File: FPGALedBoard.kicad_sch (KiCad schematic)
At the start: 5 parts, among them J1 Conn_02x20_Odd_Even

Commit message: Placa roeada automaticamente.
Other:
- company: (none) -> IFTM - Campus Ituiutaba
- title: (none) -> FPGA LED Output Board - Main
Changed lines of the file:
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@@
 (kicad_sch (version 20211123) (generator eeschema)
   (paper "A4")
+  (title_block
+    (title "FPGA LED Output Board - Main")
+    (date "2022-01-26")
+    (rev "1")
+    (company "IFTM - Campus Ituiutaba")
+  )
   (junction (at 176.53 71.12) (diameter 0) (color 0 0 0 0)
   )
@@
       (reference "#PWR0105") (unit 1) (value "+5V") (footprint "")
     )
+    (path "/ebb9e051-9d57-48fe-a44a-4edf58ab7acf/20d3631c-a610-485d-a77f-480404a55a4f"
+      (reference "#PWR0106") (unit 1) (value "GND") (footprint "")
+    )
+    (path "/ebb9e051-9d57-48fe-a44a-4edf58ab7acf/147d8636-f8cb-4d9a-9fe2-4658fd953f44"
+      (reference "#PWR0107") (unit 1) (value "+5V") (footprint "")
+    )
+    (path "/ebb9e051-9d57-48fe-a44a-4edf58ab7acf/99e75819-1ee6-4118-be75-84e1bafd18ae"
+      (reference "#PWR0108") (unit 1) (value "GND") (footprint "")
+    )
+    (path "/ebb9e051-9d57-48fe-a44a-4edf58ab7acf/51f6e505-70fe-4cfa-8e51-aa721df03c0b"
+      (reference "#PWR0109") (unit 1) (value "+5V") (footprint "")
+    )
+    (path "/b1f06ebd-9631-4b3b-9237-63ceeafca95e/b8bb4a94-4aef-4d3f-bdd0-866eb8c04d91"
+      (reference "C1") (unit 1) (value "10uF") (footprint "Capacitor_THT:CP_Radial_D5.0mm_P2.50mm")
+    )
+    (path "/b1f06ebd-9631-4b3b-9237-63ceeafca95e/dadc5b33-c8b6-468e-bb36-9ffa3f059f37"
+      (reference "C2") (unit 1) (value "10uF") (footprint "Capacitor_THT:CP_Radial_D5.0mm_P2.50mm")
+    )
+    (path "/b1f06ebd-9631-4b3b-9237-63ceeafca95e/4dff0a8e-15b6-4ad4-9af2-e1592dfea4bc"
+      (reference "C3") (unit 1) (value "10uF") (footprint "Capacitor_THT:CP_Radial_D5.0mm_P2.50mm")
+    )
+    (path "/ebb9e051-9d57-48fe-a44a-4edf58ab7acf/ada4f1f9-a877-4a31-ac0e-674903a1c441"
+      (reference "C4") (unit 1) (value "10uF") (footprint "Capacitor_THT:CP_Radial_D5.0mm_P2.50mm")
+    )
+    (path "/ebb9e051-9d57-48fe-a44a-4edf58ab7acf/fee69415-3b1b-467a-9596-a7af933deba2"
+      (reference "C5") (unit 1) (value "10uF") (footprint "Capacitor_THT:CP_Radial_D5.0mm_P2.50mm")
+    )
     (path "/b1f06ebd-9631-4b3b-9237-63ceeafca95e/bafb552e-736d-4d46-943b-7a792067c0dd"
       (reference "D1") (unit 1) (value "LED") (footprint "LED_THT:LED_D3.0mm")
@@
       (reference "U3") (unit 4) (value "74AHC04") (footprint "Package_DIP:DIP-14_W7.62mm")
     )
+    (path "/ebb9e051-9d57-48fe-a44a-4edf58ab7acf/8f177dae-7048-44cb-aed5-9ee2ed31b985"
+      (reference "U3") (unit 5) (value "74AHC04") (footprint "Package_DIP:DIP-14_W7.62mm")
+    )
+    (path "/ebb9e051-9d57-48fe-a44a-4edf58ab7acf/e32c4ea7-4f7f-485c-bc9d-52c3c4186a99"
+      (reference "U3") (unit 6) (value "74AHC04") (footprint "Package_DIP:DIP-14_W7.62mm")
+    )
     (path "/b1f06ebd-9631-4b3b-9237-63ceeafca95e/94419dcd-8a47-4346-bad9-959b3a1cf43c"
       (reference "U3") (unit 7) (value "74AHC04") (footprint "Package_DIP:DIP-14_W7.62mm")
@@
       (reference "U4") (unit 4) (value "74AHC04") (footprint "Package_DIP:DIP-14_W7.62mm")
     )
-    (path "/ebb9e051-9d57-48fe-a44a-4edf58ab7acf/8f177dae-7048-44cb-aed5-9ee2ed31b985"
+    (path "/ebb9e051-9d57-48fe-a44a-4edf58ab7acf/9775dbd4-51ad-4918-bcc6-fc67cc365ee7"
       (reference "U4") (unit 5) (value "74AHC04") (footprint "Package_DIP:DIP-14_W7.62mm")
     )
-    (path "/ebb9e051-9d57-48fe-a44a-4edf58ab7acf/e32c4ea7-4f7f-485c-bc9d-52c3c4186a99"
+    (path "/ebb9e051-9d57-48fe-a44a-4edf58ab7acf/d05b7b76-e8d1-4210-8cd0-720f16e13d24"
       (reference "U4") (unit 6) (value "74AHC04") (footprint "Package_DIP:DIP-14_W7.62mm")
+    )
+    (path "/ebb9e051-9d57-48fe-a44a-4edf58ab7acf/f01717ce-5ea2-40bb-b345-2f1eb154ce2d"
+      (reference "U4") (unit 7) (value "74AHC04") (footprint "Package_DIP:DIP-14_W7.62mm")
     )
     (path "/ebb9e051-9d57-48fe-a44a-4edf58ab7acf/cfc3b2b4-1d97-4f46-b5dc-f14c71e1a6a2"
@@
       (reference "U5") (unit 4) (value "74AHC04") (footprint "Package_DIP:DIP-14_W7.62mm")
     )
-    (path "/ebb9e051-9d57-48fe-a44a-4edf58ab7acf/9775dbd4-51ad-4918-bcc6-fc67cc365ee7"
+    (path "/ebb9e051-9d57-48fe-a44a-4edf58ab7acf/f1165d29-5632-40a1-b10d-a3067f0b2b0a"
       (reference "U5") (unit 5) (value "74AHC04") (footprint "Package_DIP:DIP-14_W7.62mm")
     )
-    (path "/ebb9e051-9d57-48fe-a44a-4edf58ab7acf/d05b7b76-e8d1-4210-8cd0-720f16e13d24"
+    (path "/ebb9e051-9d57-48fe-a44a-4edf58ab7acf/c888f29d-e025-449f-a4a4-edeed2746fde"
       (reference "U5") (unit 6) (value "74AHC04") (footprint "Package_DIP:DIP-14_W7.62mm")
+    )
+    (path "/ebb9e051-9d57-48fe-a44a-4edf58ab7acf/aebbe4a9-8276-47f3-ab49-db454bafd386"
+      (reference "U5") (unit 7) (value "74AHC04") (footprint "Package_DIP:DIP-14_W7.62mm")
     )
     (path "/ebb9e051-9d57-48fe-a44a-4edf58ab7acf/0256fd15-c8e3-42ff-8a02-4ab7ec7ac551"
       (reference "U6") (unit 1) (value "D148K") (footprint "Display_7Segment:D1X8K")
     )
-    (path "/ebb9e051-9d57-48fe-a44a-4edf58ab7acf/f1165d29-5632-40a1-b10d-a3067f0b2b0a"
-      (reference "U7") (unit 5) (value "74AHC04") (footprint "Package_DIP:DIP-14_W7.62mm")
-    )
-    (path "/ebb9e051-9d57-48fe-a44a-4edf58ab7acf/c888f29d-e025-449f-a4a4-edeed2746fde"
-      (reference "U7") (unit 6) (value "74AHC04") (footprint "Package_DIP:DIP-14_W7.62mm")
-    )
     (path "/ebb9e051-9d57-48fe-a44a-4edf58ab7acf/cc5a93cc-9281-4348-a8ca-ccf4c4a00ed9"

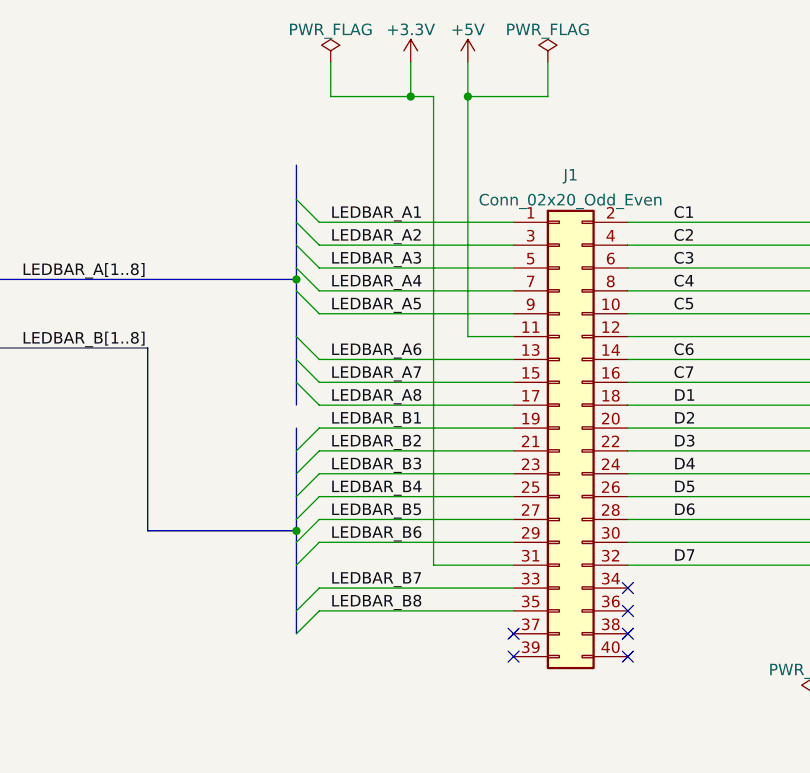
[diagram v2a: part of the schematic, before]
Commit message: Corrigido um erro na linha de 3.3V. Adicionado o Ground Plane.
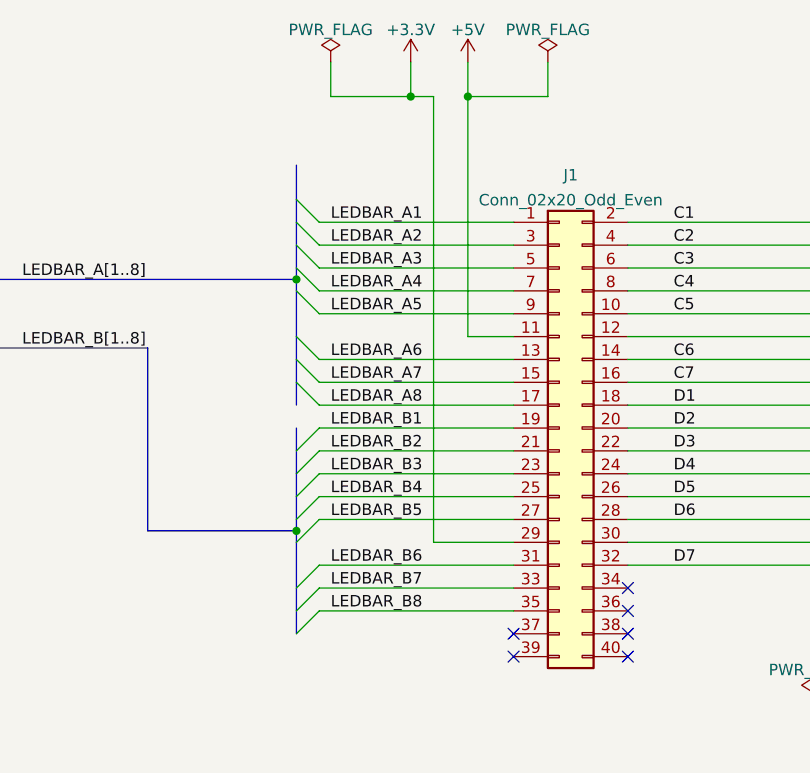
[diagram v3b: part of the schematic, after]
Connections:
- net +3V3: now also J1.29 (Pin_29); no longer J1.31 (Pin_31)
- net LEDBAR_B6: now also J1.31 (Pin_31); no longer J1.29 (Pin_29)
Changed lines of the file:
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@@
     (title "FPGA LED Output Board - Main")
     (date "2022-01-26")
-    (rev "1")
+    (rev "1.0")
     (company "IFTM - Campus Ituiutaba")
   )
@@
     (stroke (width 0) (type default) (color 0 0 0 0))
   )
-  (bus_entry (at 106.68 99.06) (size 2.54 -2.54)
+  (bus_entry (at 106.68 101.6) (size 2.54 -2.54)
     (stroke (width 0) (type default) (color 0 0 0 0))
   )
@@
     (stroke (width 0) (type default) (color 0 0 0 0))
   )
+  (wire (pts (xy 121.92 96.52) (xy 130.81 96.52))
+    (stroke (width 0) (type default) (color 0 0 0 0))
+  )
   (wire (pts (xy 143.51 63.5) (xy 173.99 63.5))
     (stroke (width 0) (type default) (color 0 0 0 0))
@@
     (stroke (width 0) (type default) (color 0 0 0 0))
   )
+  (wire (pts (xy 109.22 99.06) (xy 130.81 99.06))
+    (stroke (width 0) (type default) (color 0 0 0 0))
+  )
   (wire (pts (xy 109.22 76.2) (xy 130.81 76.2))
     (stroke (width 0) (type default) (color 0 0 0 0))
@@
     (stroke (width 0) (type default) (color 0 0 0 0))
   )
-  (wire (pts (xy 121.92 46.99) (xy 121.92 99.06))
+  (wire (pts (xy 121.92 46.99) (xy 121.92 96.52))
     (stroke (width 0) (type default) (color 0 0 0 0))
   )
@@
     (stroke (width 0) (type default) (color 0 0 0 0))
   )
-  (bus (pts (xy 106.68 99.06) (xy 106.68 104.14))
-    (stroke (width 0) (type default) (color 0 0 0 0))
-  )
-  (wire (pts (xy 121.92 99.06) (xy 130.81 99.06))
+  (bus (pts (xy 106.68 101.6) (xy 106.68 104.14))
     (stroke (width 0) (type default) (color 0 0 0 0))
   )
@@
     (stroke (width 0) (type default) (color 0 0 0 0))
   )
-  (wire (pts (xy 109.22 96.52) (xy 130.81 96.52))
-    (stroke (width 0) (type default) (color 0 0 0 0))
-  )
   (wire (pts (xy 143.51 93.98) (xy 173.99 93.98))
     (stroke (width 0) (type default) (color 0 0 0 0))
@@
     (stroke (width 0) (type default) (color 0 0 0 0))
   )
-  (bus (pts (xy 106.68 96.52) (xy 106.68 99.06))
+  (bus (pts (xy 106.68 96.52) (xy 106.68 101.6))
     (stroke (width 0) (type default) (color 0 0 0 0))
   )
@@
     (effects (font (size 1.27 1.27)) (justify left bottom))
   )
-  (label "LEDBAR_B6" (at 110.49 96.52 0)
-    (effects (font (size 1.27 1.27)) (justify left bottom))
-  )
+  (label "LEDBAR_B6" (at 110.49 99.06 0)
+    (effects (font (size 1.27 1.27)) (justify left bottom))
+  )
